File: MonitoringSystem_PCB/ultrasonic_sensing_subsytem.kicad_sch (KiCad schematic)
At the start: 36 parts, among them IC1 MAX660M_NOPB, J1 Ultrasonic_Conn_2, J3 Ultrasonic_Conn_1, U10 OPA192IDBVR, U11 TDC1000PW, U3 TDC7200PW, U5 OPA192IDBVR

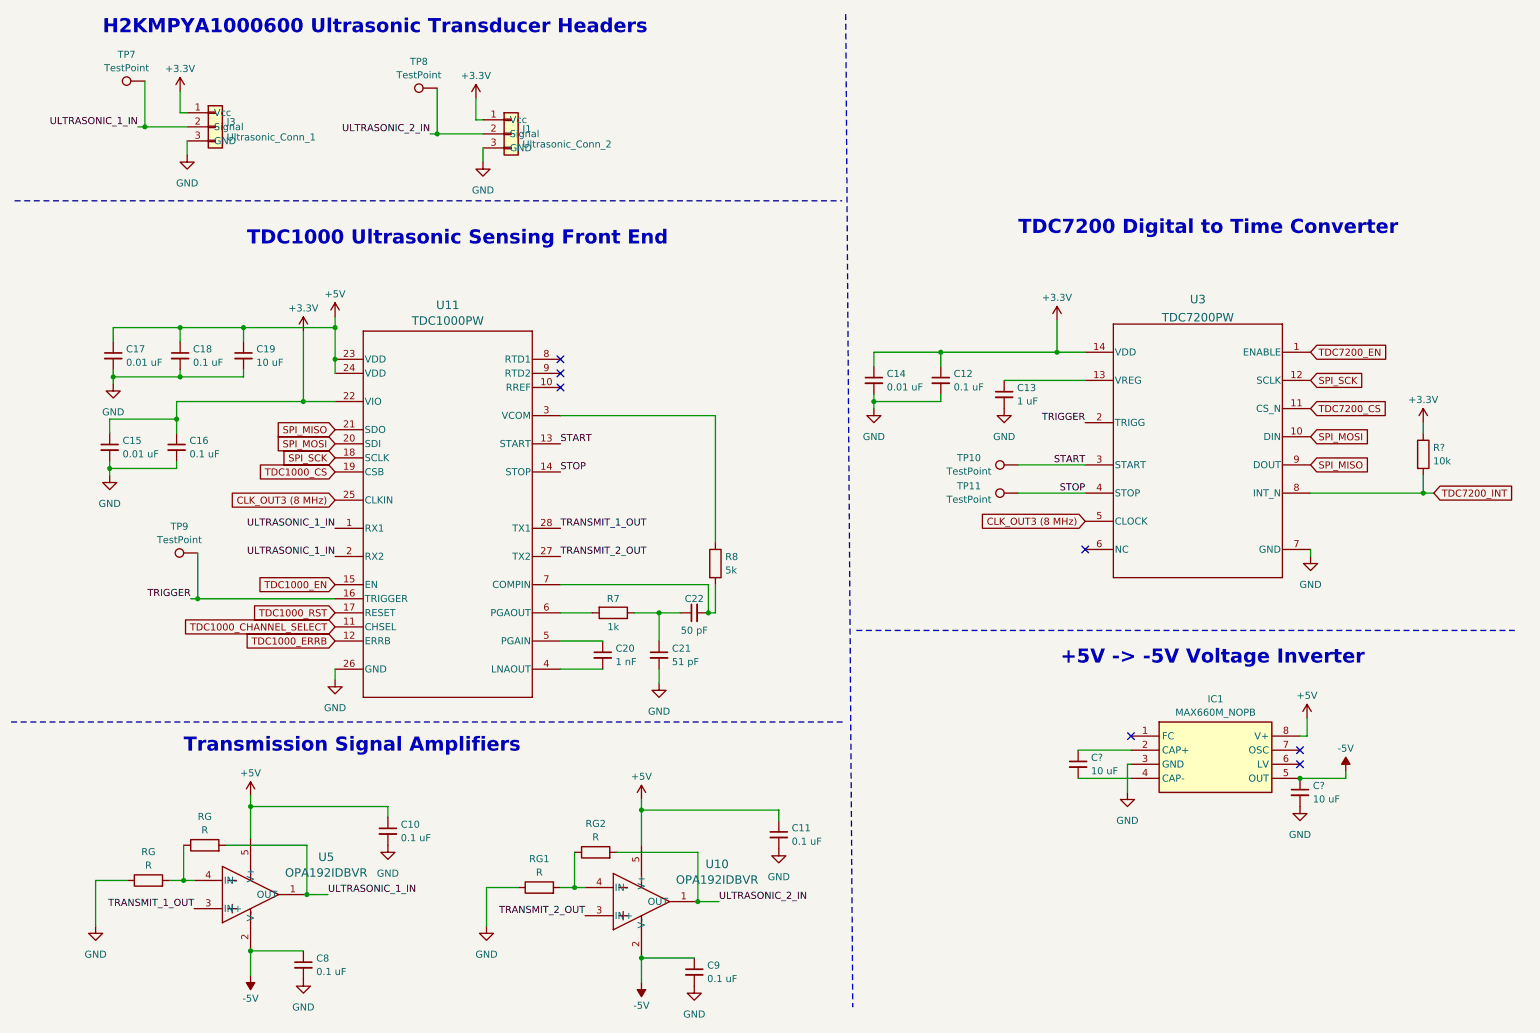
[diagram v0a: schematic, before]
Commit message: switched micro-usb for usb-b, started pcb
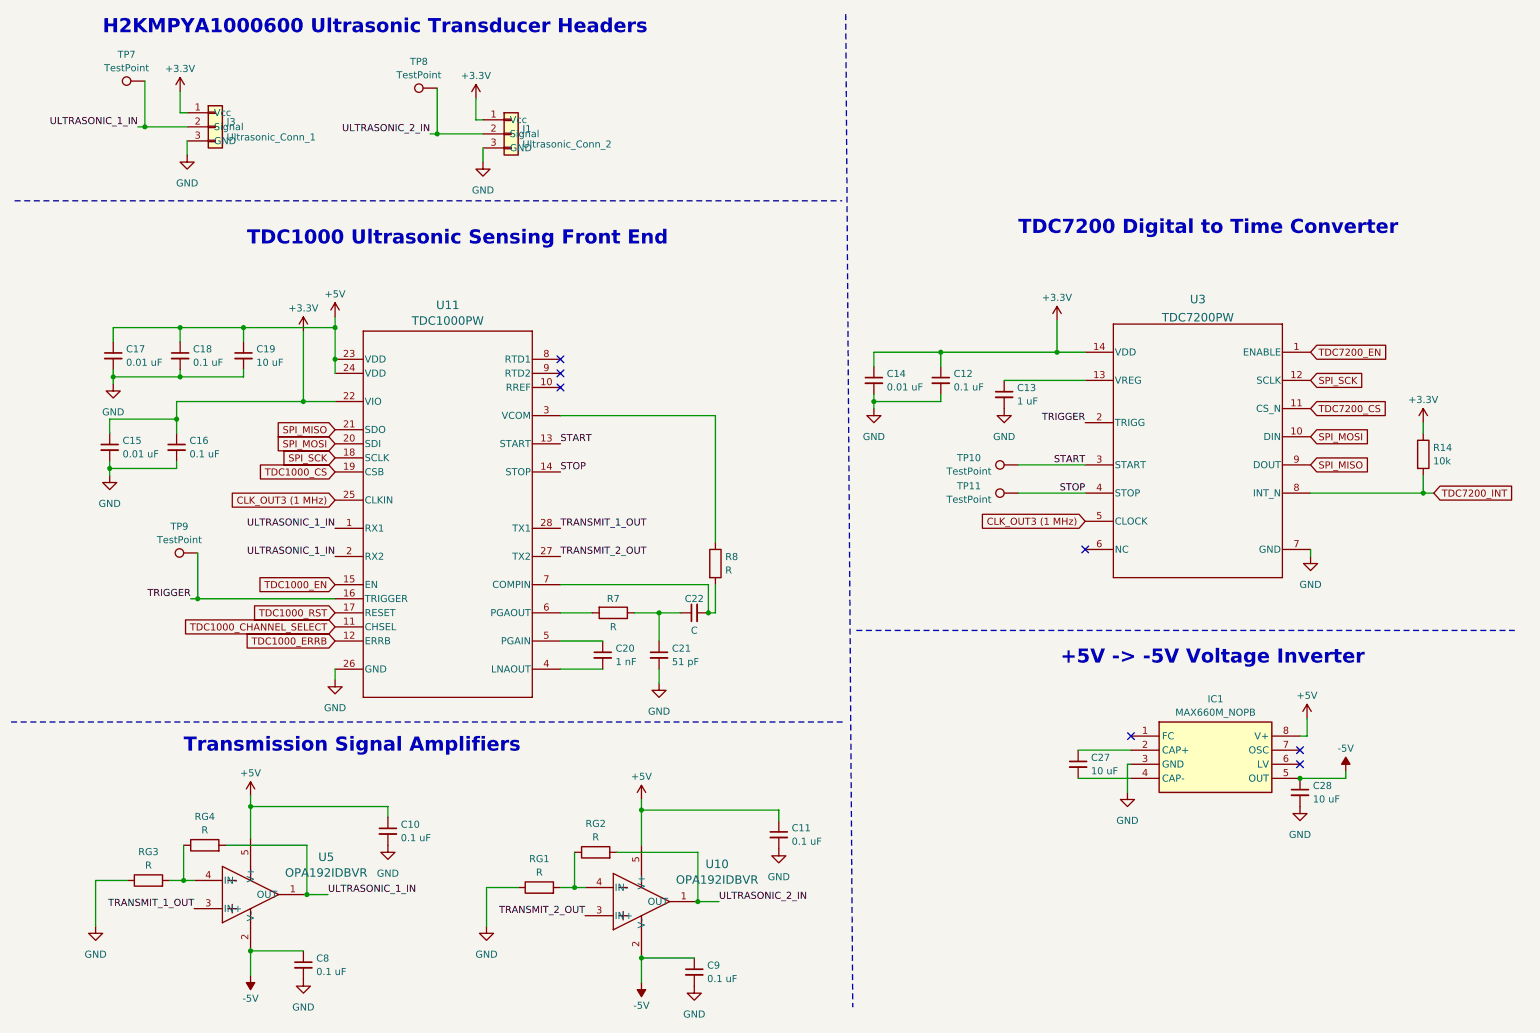
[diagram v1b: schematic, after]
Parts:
- C10, C11, C12, C13, C14, C15, C16, C17, C18, C19, C20, C21, C8, C9: footprint (none) -> Capacitor_SMD:C_0805_2012Metric
- C22: value 50 pF -> C; footprint (none) -> Capacitor_SMD:C_0805_2012Metric
- C27, C28: renamed from C?; footprint (none) -> Capacitor_SMD:C_0805_2012Metric
- IC1: footprint SOIC127P600X175-8N -> MAX660:SOIC127P600X175-8N
- J1, J3: footprint (none) -> Connector_Molex:Molex_KK-254_AE-6410-03A_1x03_P2.54mm_Vertical
- R14: renamed from R?; footprint (none) -> Resistor_SMD:R_0805_2012Metric
- R7: value 1k -> R; footprint (none) -> Resistor_SMD:R_0805_2012Metric
- R8: value 5k -> R; footprint (none) -> Resistor_SMD:R_0805_2012Metric
- RG1, RG2: footprint (none) -> Resistor_SMD:R_0805_2012Metric
- RG3, RG4: renamed from RG; footprint (none) -> Resistor_SMD:R_0805_2012Metric
- TP10, TP11, TP7, TP8, TP9: footprint (none) -> TestPoint:TestPoint_Keystone_5010-5014_Multipurpose
- U10, U5: footprint DBV0005A_N -> OPA192IDBVR Amp:DBV0005A_N
- U11: footprint PW0028A_N -> TDC1000:PW0028A_N
- U3: footprint PW0014A_N -> TDC7200:PW0014A_N
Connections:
- net CLK_OUT3 (8 MHz) renamed CLK_OUT3 (1 MHz)
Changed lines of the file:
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@@
 		)
 	)
-	(global_label "CLK_OUT3 (8 MHz)"
+	(global_label "CLK_OUT3 (1 MHz)"
 		(shape input)
 		(at 205.74 107.315 180)
@@
 		)
 	)
-	(global_label "CLK_OUT3 (8 MHz)"
+	(global_label "CLK_OUT3 (1 MHz)"
 		(shape input)
 		(at 70.485 103.505 180)
@@
 			)
 		)
-		(property "Footprint" ""
+		(property "Footprint" "TestPoint:TestPoint_Keystone_5010-5014_Multipurpose"
 			(at 88.9 24.13 0)
 			(effects
@@
 			)
 		)
-		(property "Footprint" ""
+		(property "Footprint" "TestPoint:TestPoint_Keystone_5010-5014_Multipurpose"
 			(at 193.675 97.155 0)
 			(effects
@@
 			)
 		)
-		(property "Footprint" ""
+		(property "Footprint" "TestPoint:TestPoint_Keystone_5010-5014_Multipurpose"
 			(at 193.675 92.075 0)
 			(effects
@@
 		(dnp no)
 		(fields_autoplaced yes)
-		(property "Reference" "R?"
+		(property "Reference" "R14"
 			(at 268.478 94.0378 0)
 			(effects
@@
 			)
 		)
-		(property "Footprint" ""
+		(property "Footprint" "Resistor_SMD:R_0805_2012Metric"
 			(at 264.922 95.25 90)
 			(effects
@@
 			(project "MonitoringSystem_PCB"
 				(path "/e63e39d7-6ac0-4ffd-8aa3-1841a4541b55/1f6de532-219d-4a25-a19e-57d1272e7165"
-					(reference "R?")
+					(reference "R14")
 					(unit 1)
 				)
@@
 			)
 		)
-		(property "Footprint" ""
+		(property "Footprint" "TestPoint:TestPoint_Keystone_5010-5014_Multipurpose"
 			(at 45.72 107.95 0)
 			(effects
@@
 			)
 		)
-		(property "Footprint" ""
+		(property "Footprint" "Capacitor_SMD:C_0805_2012Metric"
 			(at 150.495 163.83 0)
 			(effects
@@
 			)
 		)
-		(property "Footprint" ""
+		(property "Footprint" "TestPoint:TestPoint_Keystone_5010-5014_Multipurpose"
 			(at 36.195 22.86 0)
 			(effects
@@
 			)
 		)
-		(property "Footprint" "PW0028A_N"
+		(property "Footprint" "TDC1000:PW0028A_N"
 			(at 90.805 106.045 0)
 			(effects
@@
 			)
 		)
-		(property "Footprint" ""
+		(property "Footprint" "Capacitor_SMD:C_0805_2012Metric"
 			(at 135.255 188.595 0)
 			(effects
@@
 			)
 		)
-		(property "Footprint" ""
+		(property "Footprint" "Resistor_SMD:R_0805_2012Metric"
 			(at 117.475 168.783 90)
 			(effects
@@
 			)
 		)
-		(property "Footprint" "DBV0005A_N"
+		(property "Footprint" "OPA192IDBVR Amp:DBV0005A_N"
 			(at 120.65 170.815 0)
 			(effects
@@
 			)
 		)
-		(property "Footprint" ""
+		(property "Footprint" "Connector_Molex:Molex_KK-254_AE-6410-03A_1x03_P2.54mm_Vertical"
 			(at 48.895 36.195 0)
 			(effects
@@
 			)
 		)
-		(property "Footprint" ""
+		(property "Footprint" "Capacitor_SMD:C_0805_2012Metric"
 			(at 42.545 77.47 0)
 			(effects
@@
 			)
 		)
-		(property "Footprint" ""
+		(property "Footprint" "Capacitor_SMD:C_0805_2012Metric"
 			(at 29.845 93.98 0)
 			(effects
@@
 			)
 		)
-		(property "Footprint" ""
+		(property "Footprint" "Capacitor_SMD:C_0805_2012Metric"
 			(at 30.48 77.47 0)
 			(effects
@@
 			)
 		)
-		(property "Footprint" ""
+		(property "Footprint" "Capacitor_SMD:C_0805_2012Metric"
 			(at 191.135 84.455 0)
 			(effects
@@
 			)
 		)
-		(property "Footprint" ""
+		(property "Footprint" "Capacitor_SMD:C_0805_2012Metric"
 			(at 167.64 81.915 0)
 			(effects
@@
 		(dnp no)
 		(fields_autoplaced yes)
-		(property "Reference" "C?"
+		(property "Reference" "C28"
 			(at 246.7991 155.0041 0)
 			(effects
@@
 			)
 		)
-		(property "Footprint" ""
+		(property "Footprint" "Capacitor_SMD:C_0805_2012Metric"
 			(at 244.475 156.21 0)
 			(effects
@@
 			(project "MonitoringSystem_PCB"
 				(path "/e63e39d7-6ac0-4ffd-8aa3-1841a4541b55/1f6de532-219d-4a25-a19e-57d1272e7165"
-					(reference "C?")
+					(reference "C28")
 					(unit 1)
 				)
@@
 		(dnp no)
 		(fields_autoplaced yes)
-		(property "Reference" "RG"
+		(property "Reference" "RG4"
 			(at 46.99 160.5745 90)
 			(effects
@@
 			)
 		)
-		(property "Footprint" ""
+		(property "Footprint" "Resistor_SMD:R_0805_2012Metric"
 			(at 46.99 167.513 90)
 			(effects
@@
 			(project ""
 				(path "/e63e39d7-6ac0-4ffd-8aa3-1841a4541b55/1f6de532-219d-4a25-a19e-57d1272e7165"
-					(reference "RG")
+					(reference "RG4")
 					(unit 1)
 				)
@@
 			)
 		)
-		(property "Footprint" ""
+		(property "Footprint" "Capacitor_SMD:C_0805_2012Metric"
 			(at 179.705 81.915 0)
 			(effects
@@
 			)
 		)
-		(property "Footprint" "SOIC127P600X175-8N"
+		(property "Footprint" "MAX660:SOIC127P600X175-8N"
 			(at 240.665 240.97 0)
 			(effects
@@
 			)
 		)
-		(property "Footprint" ""
+		(property "Footprint" "Capacitor_SMD:C_0805_2012Metric"
 			(at 64.77 187.325 0)
 			(effects
@@
 			)
 		)
-		(property "Footprint" ""
+		(property "Footprint" "Capacitor_SMD:C_0805_2012Metric"
 			(at 118.745 131.445 0)
 			(effects
@@
 			)
 		)
-		(property "Value" "5k"
+		(property "Value" "R"
 			(at 140.843 116.1471 0)
 			(effects
@@
 			)
 		)
-		(property "Footprint" ""
+		(property "Footprint" "Resistor_SMD:R_0805_2012Metric"
 			(at 137.287 114.935 90)
 			(effects
@@
 			)
 		)
-		(property "Footprint" ""
+		(property "Footprint" "Capacitor_SMD:C_0805_2012Metric"
 			(at 53.975 77.47 0)
 			(effects
@@
 			)
 		)
-		(property "Footprint" "PW0014A_N"
+		(property "Footprint" "TDC7200:PW0014A_N"
 			(at 226.06 94.615 0)
 			(effects
@@
 			)
 		)
-		(property "Footprint" ""
+		(property "Footprint" "Connector_Molex:Molex_KK-254_AE-6410-03A_1x03_P2.54mm_Vertical"
 			(at 102.235 37.465 0)
 			(effects
@@
 		(dnp no)
 		(fields_autoplaced yes)
-		(property "Reference" "RG"
+		(property "Reference" "RG3"
 			(at 36.83 166.9245 90)
 			(effects
@@
 			)
 		)
-		(property "Footprint" ""
+		(property "Footprint" "Resistor_SMD:R_0805_2012Metric"
 			(at 36.83 173.863 90)
 			(effects
@@
 			(project ""
 				(path "/e63e39d7-6ac0-4ffd-8aa3-1841a4541b55/1f6de532-219d-4a25-a19e-57d1272e7165"
-					(reference "RG")
+					(reference "RG3")
 					(unit 1)
 				)
@@
 			)
 		)
-		(property "Value" "50 pF"
+		(property "Value" "C"
 			(at 135.255 127 90)
 			(effects
@@
 			)
 		)
-		(property "Footprint" ""
+		(property "Footprint" "Capacitor_SMD:C_0805_2012Metric"
 			(at 135.255 123.825 0)
 			(effects
@@
 			)
 		)
-		(property "Footprint" ""
+		(property "Footprint" "Capacitor_SMD:C_0805_2012Metric"
 			(at 128.905 131.445 0)
 			(effects
@@
 			)
 		)
-		(property "Footprint" ""
+		(property "Footprint" "Capacitor_SMD:C_0805_2012Metric"
 			(at 80.01 163.195 0)
 			(effects
@@
 			)
 		)
-		(property "Value" "1k"
+		(property "Value" "R"
 			(at 120.65 126.365 90)
 			(effects
@@
 			)
 		)
-		(property "Footprint" ""
+		(property "Footprint" "Resistor_SMD:R_0805_2012Metric"
 			(at 120.65 122.047 90)
 			(effects
@@
 		(dnp no)
 		(fields_autoplaced yes)
-		(property "Reference" "C?"
+		(property "Reference" "C27"
 			(at 206.7941 149.9241 0)
 			(effects
@@
 			)
 		)
-		(property "Footprint" ""
+		(property "Footprint" "Capacitor_SMD:C_0805_2012Metric"
 			(at 204.47 151.13 0)
 			(effects
@@
 			(project "MonitoringSystem_PCB"
 				(path "/e63e39d7-6ac0-4ffd-8aa3-1841a4541b55/1f6de532-219d-4a25-a19e-57d1272e7165"
-					(reference "C?")
+					(reference "C27")
 					(unit 1)
 				)
@@
 			)
 		)
-		(property "Footprint" "DBV0005A_N"
+		(property "Footprint" "OPA192IDBVR Amp:DBV0005A_N"
 			(at 50.165 169.545 0)
 			(effects
@@
 			)
 		)
-		(property "Footprint" ""
+		(property "Footprint" "Resistor_SMD:R_0805_2012Metric"
 			(at 107.315 175.133 90)
 			(effects
@@
 			)
 		)
-		(property "Footprint" ""
+		(property "Footprint" "Capacitor_SMD:C_0805_2012Metric"
 			(at 41.91 93.98 0)
 			(effects

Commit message: pcb done
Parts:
- C20: value 1 nF -> C
- C21: value 51 pF -> C
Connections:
- net ULTRASONIC_1_IN: no longer U11.2 (RX2)
- net ULTRASONIC_2_IN: now also U11.2 (RX2)
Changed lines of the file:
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@@
 		)
 	)
-	(label "ULTRASONIC_1_IN"
+	(label "ULTRASONIC_2_IN"
 		(at 70.485 113.665 180)
 		(fields_autoplaced yes)
@@
 			)
 		)
-		(property "Value" "1 nF"
+		(property "Value" "C"
 			(at 121.0691 132.6634 0)
 			(effects
@@
 			)
 		)
-		(property "Value" "51 pF"
+		(property "Value" "C"
 			(at 131.2291 132.6634 0)
 			(effects

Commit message: BOM and minor pcb updates
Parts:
- C20: value C -> 1 nF
- C21: value C -> 53 pF
- C22: value C -> 50 pF
- R7: value R -> 1k
- R8: value R -> 5k
- RG1, RG2, RG3, RG4: value R -> 10k
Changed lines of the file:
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@@
 			)
 		)
-		(property "Value" "R"
+		(property "Value" "10k"
 			(at 117.475 164.2688 90)
 			(effects
@@
 			)
 		)
-		(property "Value" "R"
+		(property "Value" "10k"
 			(at 46.99 162.9988 90)
 			(effects
@@
 			)
 		)
-		(property "Value" "C"
+		(property "Value" "1 nF"
 			(at 121.0691 132.6634 0)
 			(effects
@@
 			)
 		)
-		(property "Value" "R"
+		(property "Value" "5k"
 			(at 140.843 116.1471 0)
 			(effects
@@
 			)
 		)
-		(property "Value" "R"
+		(property "Value" "10k"
 			(at 36.83 169.3488 90)
 			(effects
@@
 			)
 		)
-		(property "Value" "C"
+		(property "Value" "50 pF"
 			(at 135.255 127 90)
 			(effects
@@
 			)
 		)
-		(property "Value" "C"
+		(property "Value" "53 pF"
 			(at 131.2291 132.6634 0)
 			(effects
@@
 			)
 		)
-		(property "Value" "R"
+		(property "Value" "1k"
 			(at 120.65 126.365 90)
 			(effects
@@
 			)
 		)
-		(property "Value" "R"
+		(property "Value" "10k"
 			(at 107.315 170.6188 90)
 			(effects

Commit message: most recent pcb
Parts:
- removed C10, C11: 0.1 uF, Capacitor_SMD:C_0805_2012Metric, symbol Device:C_Small
- removed C27, C28: 10 uF, Capacitor_SMD:C_0805_2012Metric, symbol Device:C_Small
- removed IC1: MAX660M_NOPB, MAX660:SOIC127P600X175-8N, symbol Voltage Inverter:MAX660M_NOPB
- removed J1: Ultrasonic_Conn_2, Connector_Molex:Molex_KK-254_AE-6410-03A_1x03_P2.54mm_Vertical, symbol Connector_Generic:Conn_01x03
- removed J3: Ultrasonic_Conn_1, Connector_Molex:Molex_KK-254_AE-6410-03A_1x03_P2.54mm_Vertical, symbol Connector_Generic:Conn_01x03
- removed RG1, RG2, RG3, RG4: 10k, Resistor_SMD:R_0805_2012Metric, symbol Device:R
- removed TP10, TP11, TP7, TP8, TP9: TestPoint, TestPoint:TestPoint_Keystone_5010-5014_Multipurpose, symbol Connector:TestPoint
- removed U10, U5: OPA192IDBVR, OPA192IDBVR Amp:DBV0005A_N, symbol OPA192 AMP:OPA192IDBVR
- added D10, D11, D8, D9: MBR0520, Diode_SMD:D_SOD-123, symbol Diode:MBR0520
- added J1, J3: Conn_01x02, Connector_Molex:Molex_KK-254_AE-6410-02A_1x02_P2.54mm_Vertical, symbol Connector_Generic:Conn_01x02
- added R22, R23: TRACE_MATCH, Resistor_SMD:R_0805_2012Metric, symbol Device:R
- added R28, R29: SPI_R, Resistor_SMD:R_0805_2012Metric, symbol Device:R
- added TP1, TP2, TP3, TP4, TP5: TestPoint, TestPoint:TestPoint_Keystone_5010-5014_Multipurpose, symbol Connector:TestPoint
- C8, C9: value 0.1 uF -> RX_GAIN
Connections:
- net +5V: now also D10.1 (K), D9.1 (K)
- net GND: now also D11.2 (A), D8.2 (A), J1.2 (Pin_2), J3.2 (Pin_2); no longer C8.2, C9.2
- net SPI_MISO: now also R28.1, R29.2; no longer U11.21 (SDO), U3.9 (DOUT)
- net START: now also TP4.1
- net STOP: now also TP5.1
- net TRIGGER: now also TP2.1
- net -5V renamed ULTRASONIC_1
- net ULTRASONIC_1: now also J1.1 (Pin_1), R22.2, TP1.1; no longer C8.1
- net TRANSMIT_1_OUT renamed TX_SIGNAL_1
- net TX_SIGNAL_1: now also R22.1
- net TRANSMIT_2_OUT renamed TX_SIGNAL_2
- net TX_SIGNAL_2: now also R23.1
- net ULTRASONIC_1_IN renamed SENSOR_RX_1
- net SENSOR_RX_1: now also C8.2, D8.1 (K), D9.2 (A)
- net ULTRASONIC_2_IN renamed SENSOR_RX_2
- net SENSOR_RX_2: now also C9.2, D10.2 (A), D11.1 (K)
- new net: R29.1, U3.9 (DOUT)
- new net: R28.2, U11.21 (SDO)
- new net ULTRASONIC_2: C8.1, J3.1 (Pin_1), R23.2, TP3.1
- no-connect marks 7 -> 4
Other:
- note removed: "+5V -> -5V Voltage Inverter"
- note removed: "Transmission Signal Amplifiers"
- moved on the sheet: C15, C16, C17, C18, C19, C20, C21, C22, R7, R8, U11
